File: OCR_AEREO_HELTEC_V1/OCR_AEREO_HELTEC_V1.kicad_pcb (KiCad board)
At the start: 2 copper layers, 113.5 x 112.5 mm, 23 parts, among them J1 INCLINOMETRO, J10 Conn_01x02_Pin, J11 Conn_01x02_Pin, J14 MODULO SD, J19 Screw_Terminal_01x02, J3 Conn_01x18_Pin, J4 Conn_01x02_Pin, J5 Conn_01x02_Pin, J6 Screw_Terminal_01x04, J7 Screw_Terminal_01x02, J8 Conn_01x02_Pin, J9 Conn_01x02_Pin, U2 MAX3232

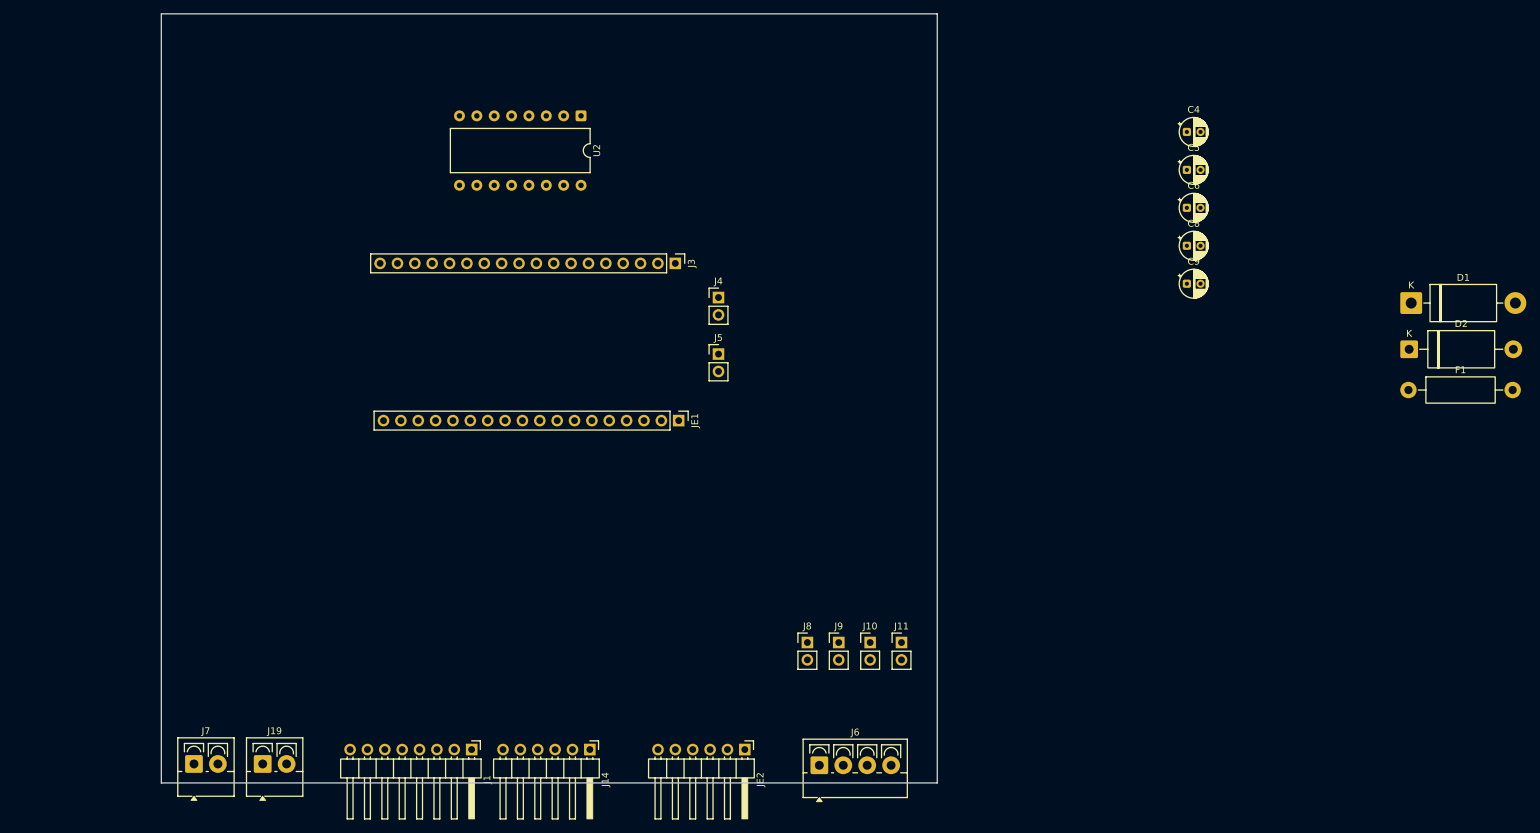
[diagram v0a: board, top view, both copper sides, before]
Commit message: Actualizacion de placa
Incluye diseño de PCB con cotas y disposición de ocmponentes actualizadas.

Incluye ambos inclinometros
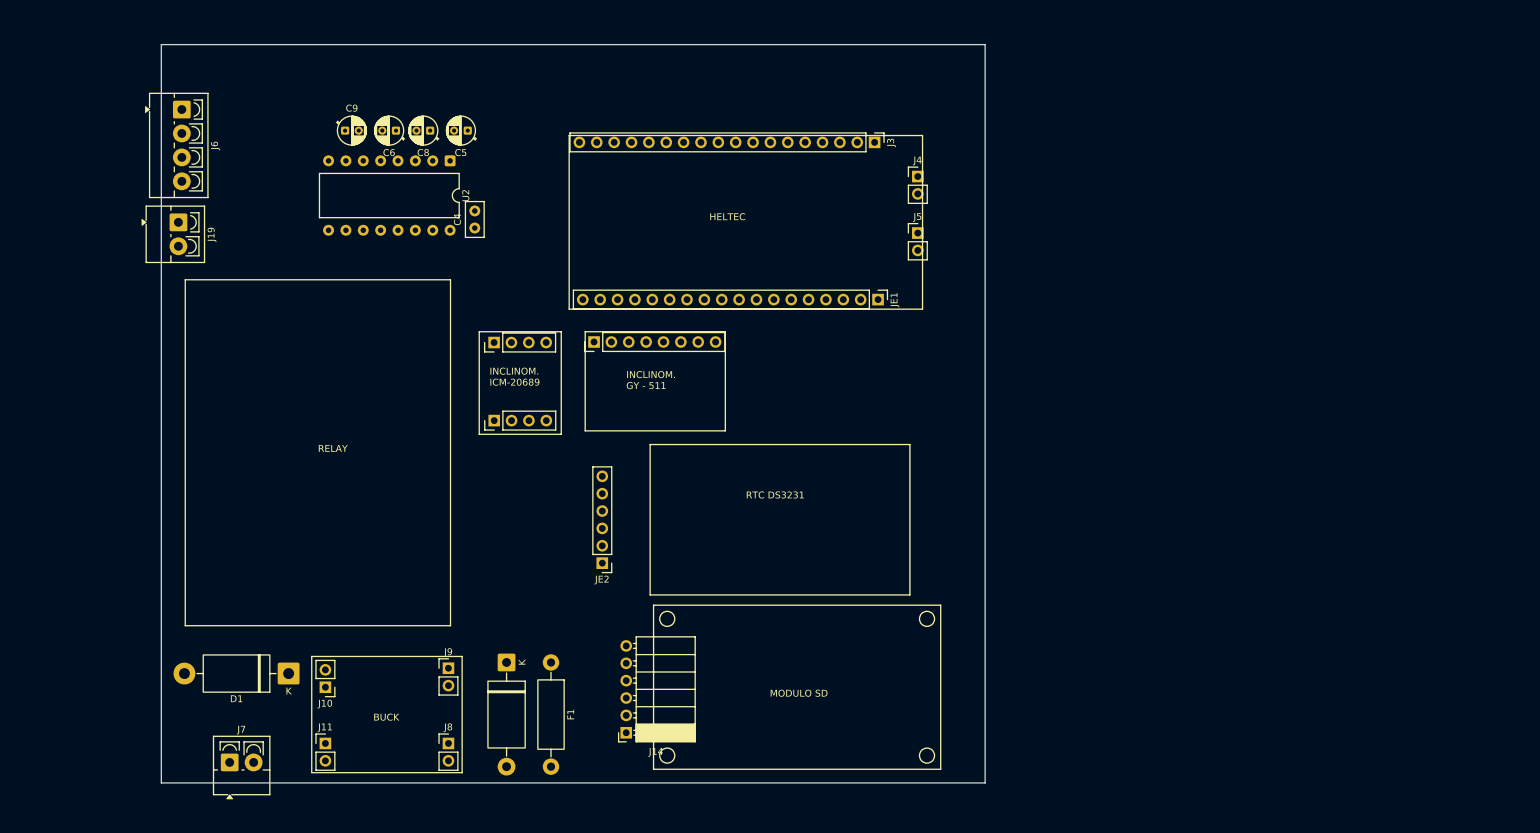
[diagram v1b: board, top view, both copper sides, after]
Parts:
- added J12: Conn_01x08_Socket, Connector_PinHeader_2.54mm:PinHeader_1x08_P2.54mm_Vertical, F.Cu at (124.8, 76.5)
- added J2: Conn_01x04_Socket, Connector_PinHeader_2.54mm:PinHeader_1x04_P2.54mm_Vertical, F.Cu at (110.2, 76.6)
- C4: footprint Capacitor_THT:CP_Radial_D4.0mm_P2.00mm -> Capacitor_THT:C_Disc_D5.0mm_W2.5mm_P2.50mm
- J1: value INCLINOMETRO -> Conn_01x04_Socket; footprint Connector_PinHeader_2.54mm:PinHeader_1x08_P2.54mm_Horizontal -> Connector_PinHeader_2.54mm:PinHeader_1x04_P2.54mm_Vertical
- J14: footprint Connector_PinHeader_2.54mm:PinHeader_1x06_P2.54mm_Horizontal -> Connector_PinSocket_2.54mm:PinSocket_1x06_P2.54mm_Horizontal
- J19: value Screw_Terminal_01x02 -> BIOSHUT
- J6: value Screw_Terminal_01x04 -> OCR
- J7: value Screw_Terminal_01x02 -> BATERÍA
- JE2: footprint Connector_PinHeader_2.54mm:PinHeader_1x06_P2.54mm_Horizontal -> Connector_PinHeader_2.54mm:PinHeader_1x06_P2.54mm_Vertical
- moved D1 172.9 mm to (80.1, 125.0), turned to 180 degrees
- moved D2 139.7 mm to (112.0, 123.4), turned to -90 degrees
- moved J6 133.8 mm to (64.5, 42.5), turned to -90 degrees
- moved F1 131.6 mm to (118.5, 123.4), turned to -90 degrees
- moved C9 125.2 mm to (88.4, 45.6)
- moved C6 116.2 mm to (95.8, 45.6), turned to 180 degrees
- moved C8 112.0 mm to (100.8, 45.6), turned to 180 degrees
- moved C5 105.3 mm to (106.3, 45.6), turned to 180 degrees
- moved C4 105.1 mm to (107.3, 59.8), turned to 90 degrees
- moved J11 85.6 mm to (85.5, 135.2)
- moved J19 80.2 mm to (64.0, 59.0), turned to -90 degrees
- moved J10 79.9 mm to (85.5, 127.0), turned to 180 degrees
- moved J9 57.2 mm to (103.5, 124.2)
- moved J8 54.5 mm to (103.5, 135.2)
- moved J1 48.2 mm to (110.2, 88.0), turned to 90 degrees
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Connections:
- J1 pad 1: unconnected-(J1-Pin_1-Pad1) -> Vext
- J1 pad 2: unconnected-(J1-Pin_2-Pad2) -> GND
- J1 pad 3: unconnected-(J1-Pin_3-Pad3) -> SCL
- J3 pad 5: unconnected-(J3-Pin_5-Pad5) -> INT_INCL
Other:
- board size 113.5 x 112.5 mm -> 120.5 x 108 mm
- board text added: "BUCK"
- board text added: "HELTEC"
- board text added: "INCLINOM. GY - 511"
- board text added: "INCLINOM. ICM-20689"
- board text added: "MODULO SD"
- board text added: "RELAY"
- board text added: "RTC DS3231"

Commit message: actualizacion V2
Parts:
- added REF**: MountingHole_2.2mm_M2, MountingHole:MountingHole_2.2mm_M2, F.Cu at (42.7, 47.5)
- added REF**: MountingHole_2.2mm_M2, MountingHole:MountingHole_2.2mm_M2, F.Cu at (42.5, 42.5)
- added REF**: MountingHole_2.2mm_M2, MountingHole:MountingHole_2.2mm_M2, F.Cu at (43.8, 118.2)
- added REF**: MountingHole_2.2mm_M2, MountingHole:MountingHole_2.2mm_M2, F.Cu at (147.0, 123.0)
- added REF**: MountingHole_3.2mm_M3, MountingHole:MountingHole_3.2mm_M3, F.Cu at (101.9, 117.5)
- added REF**: MountingHole_2.2mm_M2, MountingHole:MountingHole_2.2mm_M2, F.Cu at (80.7, 67.5)
- added REF**: MountingHole_2.2mm_M2, MountingHole:MountingHole_2.2mm_M2, F.Cu at (60.1, 118.2)
- added REF**: MountingHole_3.2mm_M3, MountingHole:MountingHole_3.2mm_M3, F.Cu at (146.4, 84.7)
- added REF**: MountingHole_2.2mm_M2, MountingHole:MountingHole_2.2mm_M2, F.Cu at (147.0, 42.5)
- added REF**: MountingHole_3.2mm_M3, MountingHole:MountingHole_3.2mm_M3, F.Cu at (101.9, 84.7)
- added REF**: MountingHole_3.2mm_M3, MountingHole:MountingHole_3.2mm_M3, F.Cu at (146.5, 117.5)
- added REF**: MountingHole_2.2mm_M2, MountingHole:MountingHole_2.2mm_M2, F.Cu at (80.7, 47.5)
- added REF**: MountingHole_2.2mm_M2, MountingHole:MountingHole_2.2mm_M2, F.Cu at (42.5, 123.0)
- added REF**: MountingHole_2.2mm_M2, MountingHole:MountingHole_2.2mm_M2, F.Cu at (42.7, 67.5)
- moved J14 93.2 mm to (86.7, 50.8), turned to 0 degrees
- moved J12 87.4 mm to (43.0, 107.3)
- moved J6 86.3 mm to (95.5, 123.0), turned to 180 degrees
- moved J4 76.8 mm to (97.6, 70.5), turned to 180 degrees
- moved C9 75.5 mm to (130.0, 108.6), turned to 180 degrees
- moved J5 74.8 mm to (97.4, 58.8)
- moved J3 68.5 mm to (103.4, 75.5), turned to 90 degrees
- moved C6 68.4 mm to (122.5, 108.6), turned to 0 degrees
- moved JE1 65.9 mm to (102.9, 52.5), turned to 90 degrees
- moved J19 65.8 mm to (78.8, 123.1), turned to 180 degrees
- moved C8 65.2 mm to (117.5, 108.6), turned to 0 degrees
- moved C5 63.3 mm to (112.0, 108.6), turned to 0 degrees
- moved J1 62.6 mm to (48.0, 95.2), turned to 0 degrees
- moved F1 60.0 mm to (66.0, 94.3)
- moved U2 55.2 mm to (114.6, 104.2), turned to 90 degrees
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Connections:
- J12 pad 2: INT_INCL -> INT_INCL_2
- J2 pad 1: INT_INCL -> INT_INCL_1
- J3 pad 5: INT_INCL -> INT_INCL_1
- J3 pad 6: unconnected-(J3-Pin_6-Pad6) -> INT_INCL_2
- J5 pad 1: unconnected-(J5-Pin_1-Pad1) -> SDA
- J5 pad 2: unconnected-(J5-Pin_2-Pad2) -> SCL
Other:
- board size 120.5 x 108 mm -> 109.5 x 85.5 mm
- board text added: "BATERIA"
- board text added: "BIOSHUT"
- board text added: "OCR"
- board text added: "X"
- board text added: "Y"

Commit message: v3 actualizada
incluye pcb routeado
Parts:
- removed J19: BIOSHUT, TerminalBlock_4Ucon:TerminalBlock_4Ucon_1x02_P3.50mm_Vertical
- added C7: 470uF, Capacitor_THT:CP_Radial_D4.0mm_P2.00mm, F.Cu at (88.0, 46.5)
- moved D1 8.51 mm to (74.4, 114.5)
- moved J7 8.25 mm to (77.2, 123.1)
- moved C8 8.23 mm to (111.5, 103.0), turned to 180 degrees
- moved C5 4.50 mm to (116.5, 108.5)
- moved J12 1.55 mm to (44.5, 107.5)
- moved REF** 1.55 mm to (45.3, 118.4)
- moved REF** 1.55 mm to (61.7, 118.4)
- moved F1 0.50 mm to (66.5, 94.3)
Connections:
- D2 pad 1: 3.3V -> 5V
- F1 pad 1: 3.3V -> 5V
- J14 pad 1: Vext -> GND
- J14 pad 2: CS_SD -> 5V
- J14 pad 3: MOSI -> MISO
- J14 pad 4: CLK_SPI -> MOSI
- J14 pad 5: MISO -> CLK_SPI
- J14 pad 6: GND -> CS_SD
- J3 pad 17: 3.3V -> unconnected-(J3-Pin_17-Pad17)
- JE1 pad 17: unconnected-(JE1-Pin_17-Pad17) -> 5V
- JE1 pad 3: MISO -> CLK_SPI
- JE1 pad 4: CLK_SPI -> MOSI
- JE1 pad 5: MOSI -> MISO
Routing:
- net 5V: track 0.00 -> 186.6 mm
- net Vext: track 0.00 -> 161.0 mm
- net INT_INCL_2: track 0.00 -> 136.1 mm
- net SDA: track 0.00 -> 100.4 mm
- net SCL: track 0.00 -> 89.4 mm
- net TX_OCR: track 0.00 -> 69.3 mm
- net INT_INCL_1: track 0.00 -> 65.5 mm
- net RX_OCR: track 0.00 -> 44.4 mm
- net MISO: track 0.00 -> 34.9 mm
- net CS_SD: track 0.00 -> 34.3 mm
- net MOSI: track 0.00 -> 31.4 mm
- net HELTEC_TO_OCR: track 0.00 -> 28.7 mm
- net OCR_TO_HELTEC: track 0.00 -> 28.7 mm
- net CLK_SPI: track 0.00 -> 26.9 mm
- net OUT_BUCK: track 0.00 -> 26.6 mm
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- added copper zone on B.Cu, net GND
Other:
- board text removed: "BIOSHUT"
